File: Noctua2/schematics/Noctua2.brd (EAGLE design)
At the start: 30 x 62 mm, 44 parts, among them IC3 STM32H750VBT6, U2 PCM3168A, U3 TLV1117LV33DCYR, X1 53048-05, Y1 8MHz

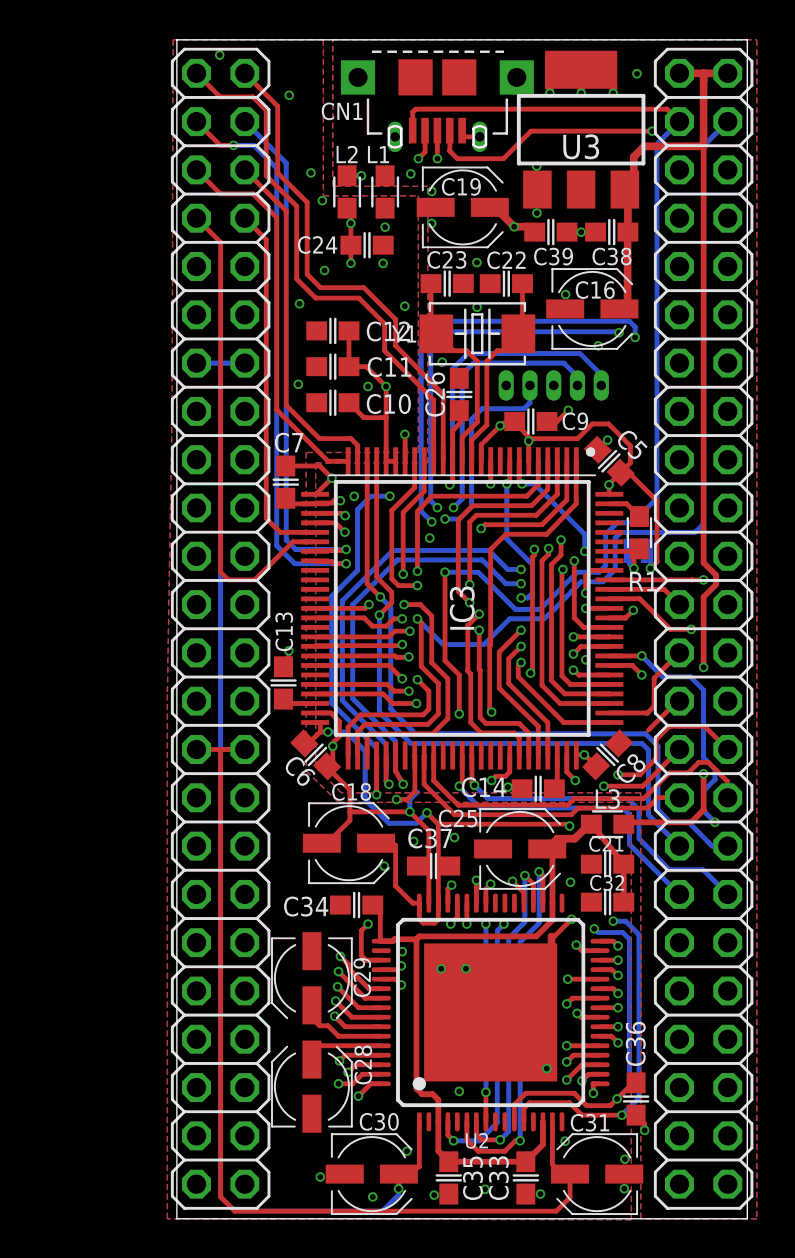
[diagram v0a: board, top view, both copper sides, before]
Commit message: deleted tracks that need to be re-routed and tracked around ADC
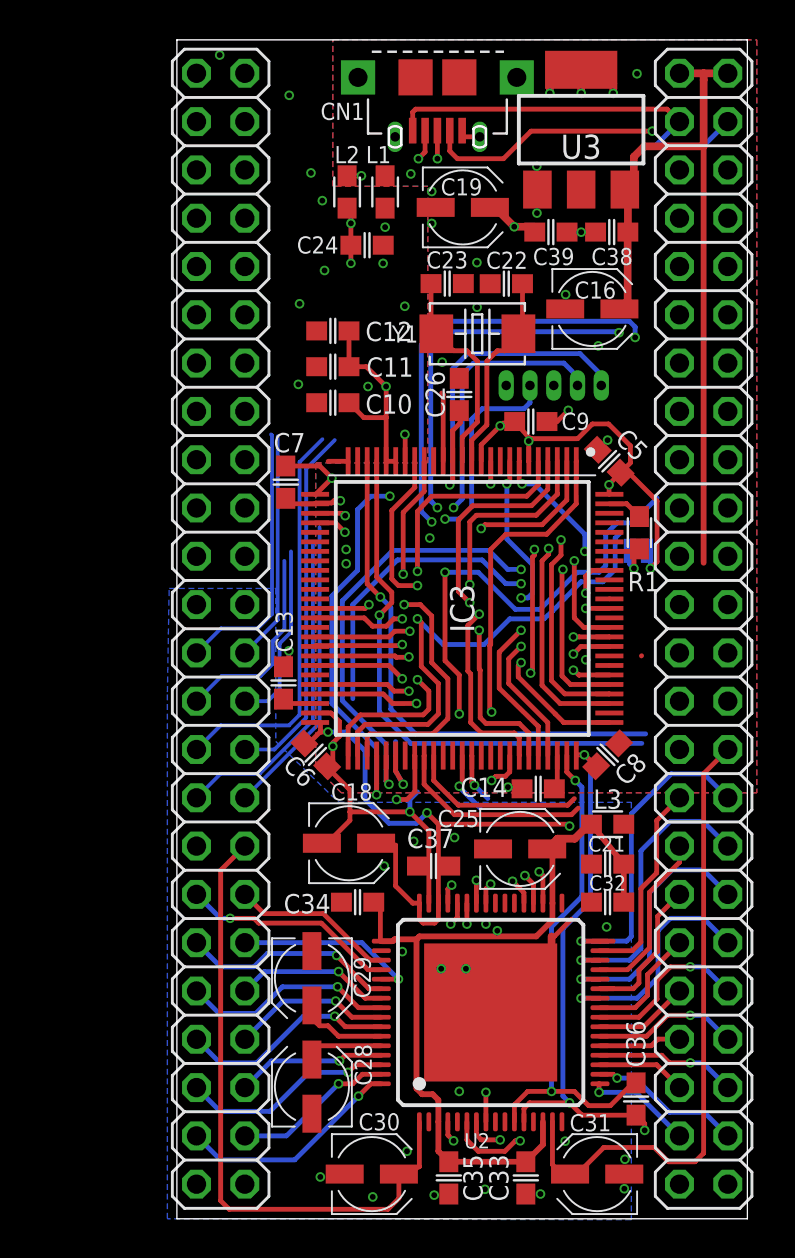
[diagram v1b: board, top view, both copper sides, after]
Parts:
- moved C34 0.16 mm to (9.80, 16.6)
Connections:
- net +3V3: now also JP1.1, JP1.2; no longer JP2.46
- net ADC1: now also JP1.25; no longer JP1.1
- net ADC2: now also JP1.27; no longer JP1.3
- net ADC3: now also JP1.29; no longer JP1.5
- net ADC4: now also JP1.31; no longer JP1.7
- net ADC5: now also JP1.26; no longer JP1.2
- net ADC6: now also JP1.28; no longer JP1.4
- net ADC7: now also JP1.30; no longer JP1.6
- net ADC8: now also JP1.32; no longer JP1.8
- net ADCREF: now also JP1.34; no longer JP1.13, JP1.14
- net AGND: now also JP1.33, JP2.25, JP2.26, JP2.29, JP2.47, JP2.48; no longer JP1.11, JP1.12, JP1.27, JP1.28
- net AIN1+: now also JP1.35; no longer JP1.15
- net AIN1-: now also JP1.36; no longer JP1.16
- net AIN2+: now also JP1.37; no longer JP1.17
- net AIN2-: now also JP1.38; no longer JP1.18
- net AIN3+: now also JP1.39; no longer JP1.19
- net AIN3-: now also JP1.40; no longer JP1.20
- net AIN4+: now also JP1.41; no longer JP1.21
- net AIN4-: now also JP1.42; no longer JP1.22
- net AIN5+: now also JP1.43; no longer JP1.23
- net AIN5-: now also JP1.44; no longer JP1.24
- net AIN6+: now also JP1.45; no longer JP1.25
- net AIN6-: now also JP1.46; no longer JP1.26
- net AOUT1+: now also JP2.31; no longer JP1.31
- net AOUT1-: now also JP2.32; no longer JP1.32
- net AOUT2+: now also JP2.33; no longer JP1.33
- net AOUT2-: now also JP2.34; no longer JP1.34
- net AOUT3+: now also JP2.35; no longer JP1.35
- net AOUT3-: now also JP2.36; no longer JP1.36
- net AOUT4+: now also JP2.37; no longer JP1.37
- net AOUT4-: now also JP2.38; no longer JP1.38
- net AOUT5+: now also JP2.39; no longer JP1.39
- net AOUT5-: now also JP2.40; no longer JP1.40
- net AOUT6+: now also JP2.41; no longer JP1.41
- net AOUT6-: now also JP2.42; no longer JP1.42
- net AOUT7+: now also JP2.43; no longer JP1.43
- net AOUT7-: now also JP2.44; no longer JP1.44
- net AOUT8+: now also JP2.45; no longer JP1.45
- net AOUT8-: now also JP2.46; no longer JP1.46
- net DAC1: now also JP2.27; no longer JP1.9
- net DAC2: now also JP2.28; no longer JP1.10
- net DACREF: now also JP2.30; no longer JP1.29, JP1.30
- net EXTI1: now also JP1.3; no longer JP2.37
- net EXTI2: now also JP1.5; no longer JP2.39
- net EXTI3: now also JP1.7; no longer JP2.41
- net EXTI4: now also JP1.9; no longer JP2.43
- net EXTI5: now also JP1.4; no longer JP2.38
- net EXTI6: now also JP1.6; no longer JP2.40
- net EXTI7: now also JP1.8; no longer JP2.42
- net EXTI8: now also JP1.10; no longer JP2.44
- net GND: now also JP1.15, JP1.16; no longer JP2.27, JP2.28, JP2.48
- net I2C_SCL: now also JP2.23; no longer JP2.45
- net I2C_SDA: now also JP2.24; no longer JP2.47
- net SPI3_MISO: now also JP2.20; no longer JP2.16
- net SPI3_MOSI: now also JP2.22; no longer JP2.18
- net SPI3_SCK: now also JP2.18; no longer JP2.14
- net SPI4_MISO: now also JP2.19; no longer JP2.15
- net SPI4_MOSI: now also JP2.21; no longer JP2.17
- net SPI4_SCK: now also JP2.17; no longer JP2.13
- net TIM1_CH1: now also JP1.11; no longer JP2.23
- net TIM1_CH2: now also JP1.12; no longer JP2.24
- net TIM2_CH1: now also JP1.13; no longer JP2.25
- net TIM2_CH2: now also JP1.14; no longer JP2.26
- net TIM3_CH1: no longer JP2.29
- net TIM3_CH2: no longer JP2.30
- net TIM4_CH1: no longer JP2.31
- net TIM4_CH2: no longer JP2.32
- net TIM5_CH1: no longer JP2.33
- net TIM5_CH2: no longer JP2.34
- net TIM6_CH1: no longer JP2.35
- net TIM6_CH2: no longer JP2.36
- net UART1_RX: now also JP2.15; no longer JP2.21
- net UART1_TX: now also JP2.13; no longer JP2.19
- net UART2_RX: now also JP2.16; no longer JP2.22
- net UART2_TX: now also JP2.14; no longer JP2.20
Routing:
- net TIM3_CH2: track 33.0 -> 5.11 mm, vias 2 -> 1
- net ADCREF: track 61.0 -> 33.8 mm, vias 1 -> 0
- net I2C_SDA: track 43.0 -> 16.3 mm
- net EXTI8: track 26.5 -> 0.00 mm, vias 1 -> 0
- net AIN1+: track 37.7 -> 11.4 mm
- net TIM3_CH1: track 30.9 -> 4.92 mm, vias 2 -> 1
- net EXTI3: track 25.6 -> 0.02 mm, vias 2 -> 0
- net AOUT4+: track 31.8 -> 6.24 mm, vias 1 -> 0
- net AOUT5+: track 29.7 -> 4.96 mm, vias 1 -> 0
- net AIN1-: track 33.3 -> 8.61 mm, vias 1 -> 0
- net I2C_SCL: track 41.0 -> 16.4 mm
- net AIN2-: track 33.8 -> 9.78 mm
- net EXTI4: track 27.6 -> 4.73 mm
- net AIN2+: track 34.0 -> 11.3 mm
- net DAC1: track 24.2 -> 1.63 mm
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- removed copper zone on layer 1, net AGND
- removed copper zone on layer 15, net AGND
- removed copper zone on layer 2, net AGND

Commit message: Tracked all of board apart from TIMs and EXTIs
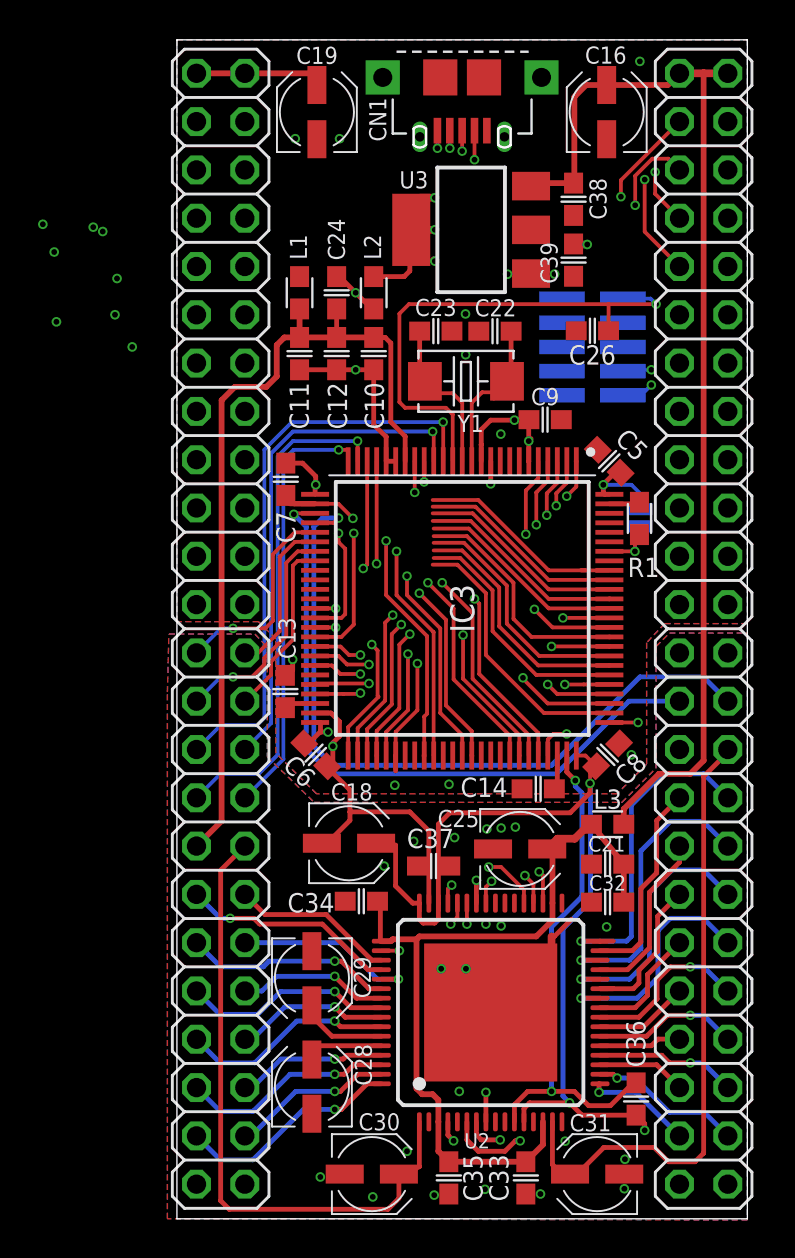
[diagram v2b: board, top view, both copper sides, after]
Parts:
- removed X1: 53048-05, con-molex:53048-05
- added J1: FTS-105-01-F-DV, borkedlabs-connectors:2X5_1.27MM_SMD
- moved C16 10.4 mm to (22.9, 58.2), turned to 90 degrees
- moved C19 9.16 mm to (7.66, 58.2), turned to 90 degrees
- moved U3 7.82 mm to (15.8, 52.0), turned to 90 degrees
- moved C26 7.76 mm to (22.1, 46.7), turned to 180 degrees
- moved L1 6.95 mm to (6.75, 48.7)
- moved L2 5.48 mm to (10.7, 48.7)
- moved C10 3.36 mm to (10.7, 45.5), turned to 90 degrees
- moved C24 2.97 mm to (8.70, 48.7), turned to 270 degrees
- moved C38 2.65 mm to (21.2, 53.6), turned to 90 degrees
- moved C22 2.57 mm to (17.0, 46.7)
- moved C23 2.57 mm to (13.9, 46.7)
- moved Y1 2.57 mm to (15.5, 44.0)
- moved C39 1.90 mm to (21.2, 50.4), turned to 270 degrees
- moved C11 1.88 mm to (6.75, 45.5), turned to 90 degrees
- moved BOOT 1.75 mm to (24.7, 36.9), turned to 270 degrees
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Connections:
- removed net SWCLK: IC3.76, X1.2
- new net SWDCLK: IC3.76, J1.4
- net +3V3: now also J1.1; no longer X1.1
- net ADC1: now also JP1.30; no longer JP1.25
- net ADC2: now also JP1.28; no longer JP1.27
- net ADC3: now also JP1.32; no longer JP1.29
- net ADC4: now also JP1.26; no longer JP1.31
- net ADC5: now also JP1.29; no longer JP1.26
- net ADC6: now also JP1.27; no longer JP1.28
- net ADC7: now also JP1.31; no longer JP1.30
- net ADC8: now also JP1.25; no longer JP1.32
- net ADC_SPI_NCS: now also IC3.40; no longer IC3.58
- net GND: now also J1.3, J1.5, J1.7, J1.9; no longer X1.3
- net NRST: now also J1.10; no longer X1.5
- net SWDIO: now also J1.2; no longer X1.4
- net TIM3_CH1: now also JP1.17
- net TIM3_CH2: now also JP1.18
- net TIM4_CH1: now also JP1.19
- net TIM4_CH2: now also JP1.20
- net TIM5_CH1: now also JP1.21
- net TIM5_CH2: now also JP1.22
- net TIM6_CH1: now also JP1.23
- net TIM6_CH2: now also JP1.24
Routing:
- net AGND: track 6.26 -> 50.7 mm, vias 29 -> 23
- net DAC2: track 1.78 -> 39.0 mm
- net DAC1: track 1.63 -> 35.5 mm
- net SWCLK: track 28.0 -> 0.00 mm, vias 2 -> 0
- net SWDCLK: track 0.00 -> 22.3 mm, vias 0 -> 2
- net TIM6_CH1: track 3.28 -> 22.3 mm
- net TIM6_CH2: track 2.61 -> 19.4 mm
- net EXTI7: track 16.1 -> 0.00 mm, vias 3 -> 0
- net UART1_RX: track 0.00 -> 15.9 mm, vias 0 -> 1
- net TIM5_CH2: track 27.5 -> 12.4 mm
- net TIM4_CH1: track 10.4 -> 25.4 mm, vias 0 -> 1
- net ADC5: track 15.7 -> 30.4 mm, vias 0 -> 1
- net TIM2_CH1: track 0.00 -> 14.4 mm
- net UART1_TX: track 6.84 -> 20.4 mm
- net +5V: track 44.4 -> 58.0 mm
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- added copper zone on layer 1, net AGND
- added copper zone on layer 15, net AGND
- added copper zone on layer 2, net AGND
- removed copper zone on layer 2, net +A3V3

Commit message: tracking complete
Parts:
- moved L1 27.0 mm to (6.10, 21.8)
- moved C22 0.30 mm to (17.3, 46.7)
- moved C23 0.20 mm to (13.7, 46.7)
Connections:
- net ADC1 renamed ADC_IN11
- net ADC2 renamed ADC_IN8
- net ADC3 renamed ADC_IN15
- net ADC4 renamed ADC_IN7
- net ADC5 renamed ADC_IN10
- net ADC6 renamed ADC_IN4
- net ADC7 renamed ADC_IN14
- net ADC8 renamed ADC_IN3
- net TIM2_CH1 renamed TIM2_CH1_EXTI15
- net TIM2_CH2 renamed TIM2_CH2_EXTI3
- net TIM6_CH1 renamed TIM8_CH1
- net TIM6_CH2 renamed TIM8_CH2
- removed net EXTI3: IC3.83, JP1.7
- removed net EXTI5: IC3.7, JP1.4
- removed net TIM1_CH1: IC3.90, JP1.11
- removed net TIM1_CH2: IC3.91, JP1.12
- removed net UART1_RX: IC3.87, JP2.15
- removed net UART1_TX: IC3.86, JP2.13
- new net EXTI0: IC3.81, JP1.9
- new net EXTI14: IC3.8, JP1.4
- new net TIM1_CH1_EXTI9: IC3.39, JP1.11
- new net TIM1_CH2_EXTI11: IC3.41, JP1.12
- new net UART3_RX: IC3.56, JP2.16
- new net UART3_TX: IC3.55, JP2.14
- net EXTI1: now also IC3.82, JP1.10; no longer IC3.92, JP1.3
- net EXTI2: now also IC3.83, JP1.7; no longer IC3.85, JP1.5
- net EXTI4: now also IC3.85, JP1.5; no longer IC3.81, JP1.9
- net EXTI6: now also IC3.92; no longer IC3.88
- net EXTI7: now also IC3.88; no longer IC3.8
- net EXTI8: now also IC3.95, JP1.3; no longer IC3.82, JP1.10
- net TIM3_CH1: now also IC3.90; no longer IC3.39
- net TIM3_CH2: now also IC3.91; no longer IC3.41
- net UART2_RX: now also IC3.87, JP2.15; no longer IC3.56, JP2.16
- net UART2_TX: now also IC3.86, JP2.13; no longer IC3.55, JP2.14
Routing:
- net EXTI0: track 0.00 -> 35.8 mm, vias 0 -> 1
- net EXTI7: track 0.00 -> 32.1 mm, vias 0 -> 1
- net UART3_TX: track 0.00 -> 32.0 mm, vias 0 -> 1
- net UART3_RX: track 0.00 -> 30.0 mm, vias 0 -> 1
- net EXTI14: track 0.00 -> 29.1 mm, vias 0 -> 1
- net EXTI4: track 13.0 -> 38.6 mm, vias 0 -> 1
- net EXTI8: track 13.0 -> 37.3 mm, vias 0 -> 1
- net EXTI2: track 12.6 -> 36.5 mm, vias 0 -> 1
- net TIM1_CH1_EXTI9: track 0.00 -> 22.6 mm, vias 0 -> 1
- net EXTI6: track 11.0 -> 33.4 mm, vias 0 -> 1
- net TIM1_CH2_EXTI11: track 0.00 -> 21.8 mm, vias 0 -> 1
- net EXTI1: track 11.1 -> 32.6 mm, vias 0 -> 1
- net UART1_TX: track 20.4 -> 0.00 mm, vias 1 -> 0
- net TIM2_CH1_EXTI15: track 14.4 -> 34.1 mm, vias 0 -> 1
- net UART1_RX: track 15.9 -> 0.00 mm, vias 1 -> 0
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
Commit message: changed labels, Noctua2 Rev01
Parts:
- renumbered IC3 to U1
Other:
- board text added: "76"
- board text added: "Noctua2 Rev01"
- board text removed: "78"
- board text removed: "82"
- board text removed: "84"
- board text removed: "86"
- board text removed: "Xibeca Rev03"
